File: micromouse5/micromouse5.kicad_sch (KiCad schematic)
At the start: 21 parts, among them J1 Conn_01x06_Pin, J2 Conn_01x06_Pin, J3 JST 2, J4 JST 1, Q1 IR Receiver, U1 HBridge, U2 Voltage Regulator, U3 MOSFET

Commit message: fix naming
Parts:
- R1: footprint micromouse5:BO_CR0805 -> micromouse5:BO_CR0805(51 ohm)
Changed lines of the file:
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@@
 			)
 		)
-		(property "Footprint" "micromouse5:BO_CR0805"
+		(property "Footprint" "micromouse5:BO_CR0805(51 ohm)"
 			(at 237.49 97.79 0)
 			(effects

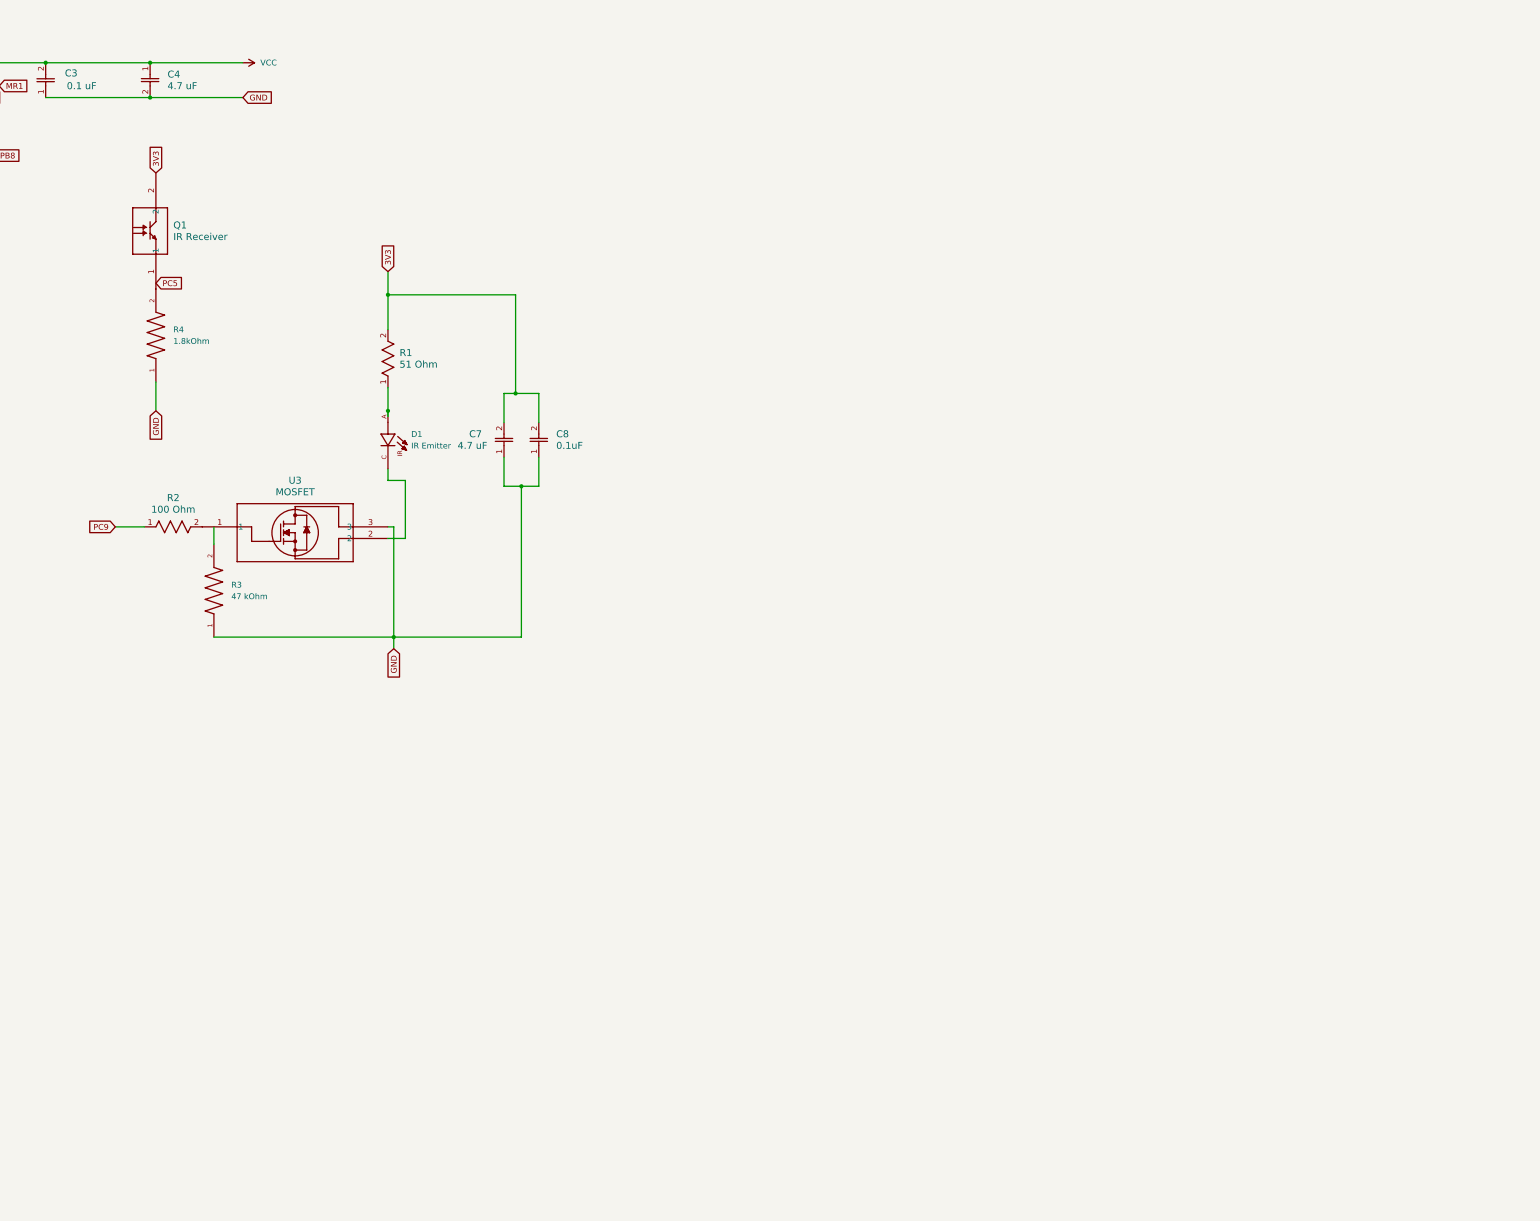
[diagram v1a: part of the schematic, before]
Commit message: Increased size of schematic and created groups/text labels
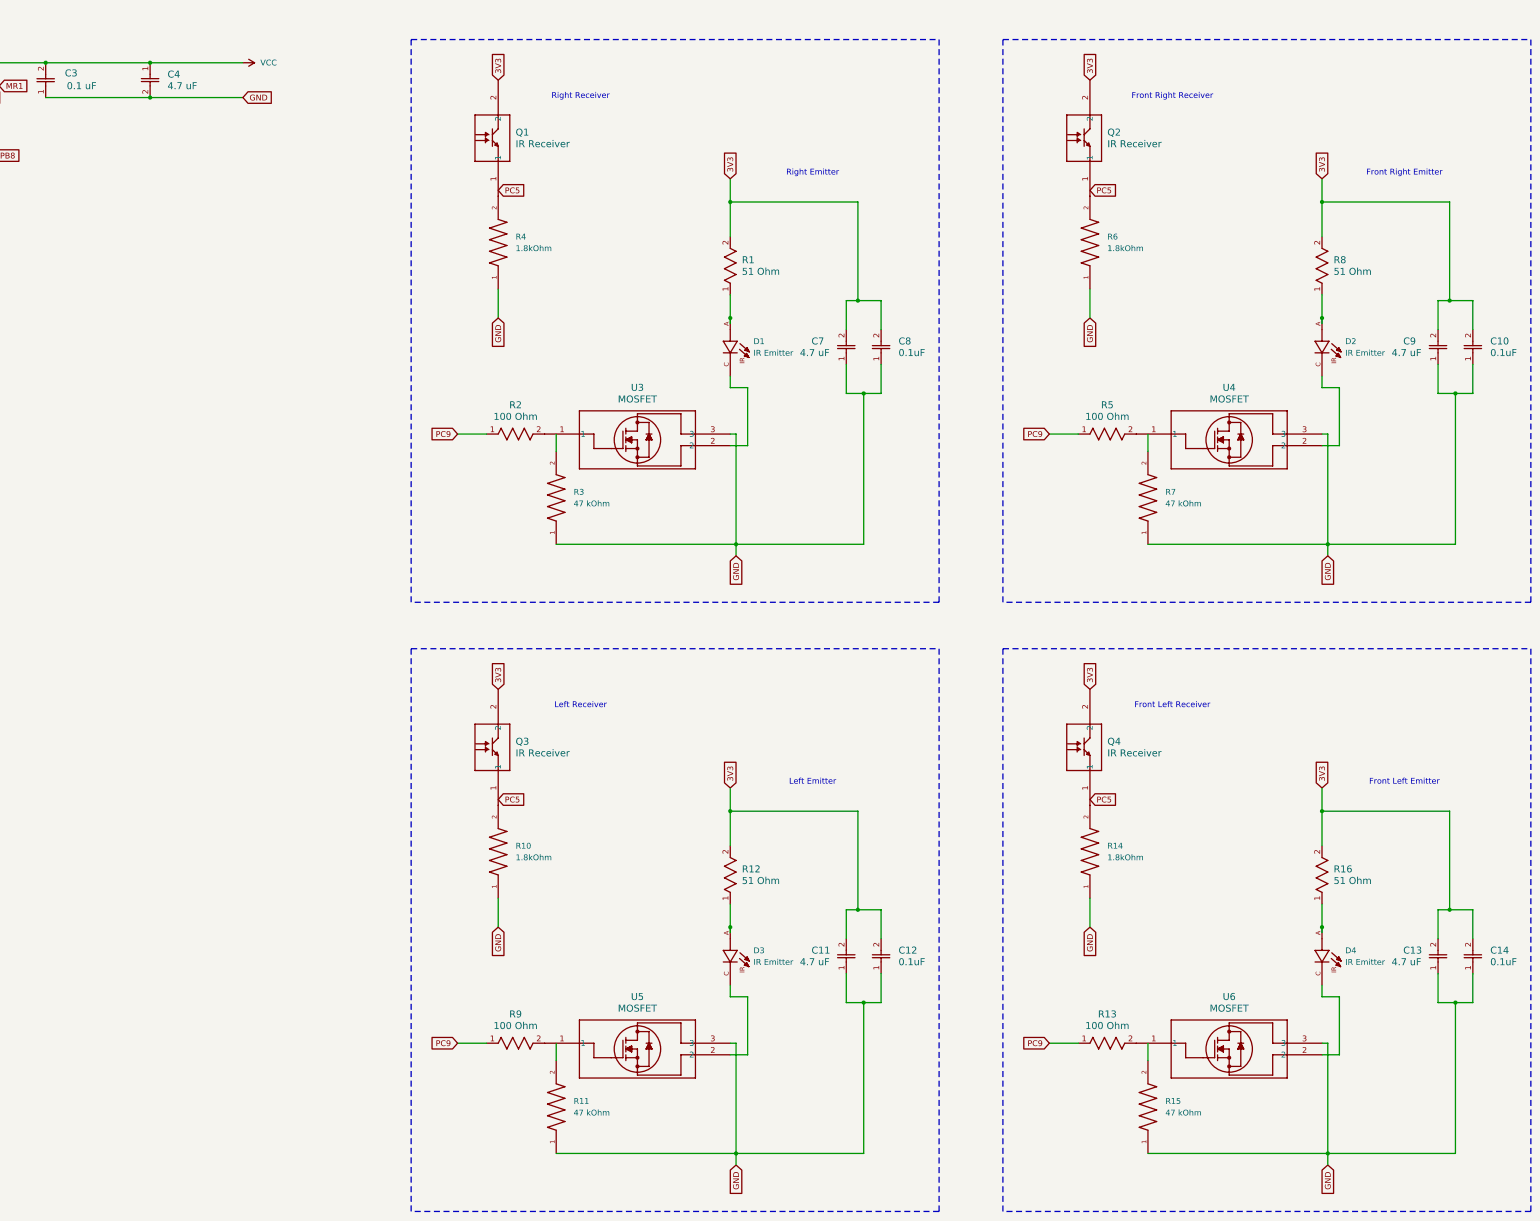
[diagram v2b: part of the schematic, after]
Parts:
- added C10, C12, C14: 0.1uF, micromouse5:G-21_MUR(0.1), symbol Capacitor-0.1uF:GRM21BR71C475KE51L
- added C11, C13, C9: 4.7 uF, micromouse5:CAP_GRM0805_2X1P25_MUR, symbol Capacitor-4.7uF:GCJ21BR72A104KA01L
- added D2, D3, D4: IR Emitter, micromouse5:DIO_SFH_4545 (IR- Emitter), symbol IR-Emitter:SFH_4545
- added Q2, Q3, Q4: IR Receiver, micromouse5:NoneP157X157-2_LTO (IR- Receiver), symbol IR-Receiver:LTR-4206E
- added R10, R14, R6: 1.8kOhm, micromouse5:RESC2012X60N (1.8kΩ), symbol Resistor- 1.8kohm:RK73H2ATTD1801F
- added R11, R15, R7: 47 kOhm, micromouse5:RESC2012X60N (47kΩ), symbol Resistor- 47kohm:RK73H2ARTTD4702F
- added R12, R16, R8: 51 Ohm, micromouse5:BO_CR0805(51 ohm), symbol CRM0805-FX-51R0ELF (51 ohm):CRM0805-FX-51R0ELF
- added R13, R5, R9: 100 Ohm, micromouse5:STA_RNCP0805_STP(100 ohm), symbol RNCP0805FTD100R(100 resistor):RNCP0805FTD100R
- added U4, U5, U6: MOSFET, micromouse5:SOT-23_3L_ONS (mosfet), symbol Mosfet:2N7002LT1G
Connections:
- net 3V3: now also C10.2, C11.2, C12.2, C13.2, C14.2, C9.2, Q2.2, Q3.2, Q4.2, R12.2, R16.2, R8.2
- net GND: now also C10.1, C11.1, C12.1, C13.1, C14.1, C9.1, R10.1, R11.1, R14.1, R15.1, R6.1, R7.1, U4.3, U5.3, U6.3
- net PC9: now also R13.1, R5.1, R9.1
- new net: D4.A, R16.1
- new net: D4.C, U6.2
- new net: Q4.1, R14.2
- new net: D3.A, R12.1
- new net: D3.C, U5.2
- new net: R5.2, U4.1
- new net: D2.C, U4.2
- new net: Q2.1, R6.2
- new net: R13.2, U6.1
- new net: R9.2, U5.1
- new net: D2.A, R8.1
- new net: Q3.1, R10.2
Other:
- note added: "Front Left Emitter"
- note added: "Front Left Receiver"
- note added: "Front Right Emitter"
- note added: "Front Right Receiver"
- note added: "Left Emitter"
- note added: "Left Receiver"
- note added: "Right Emitter"
- note added: "Right Receiver"
- moved on the sheet: C7, C8, D1, Q1, R1, R2, R3, R4, U3

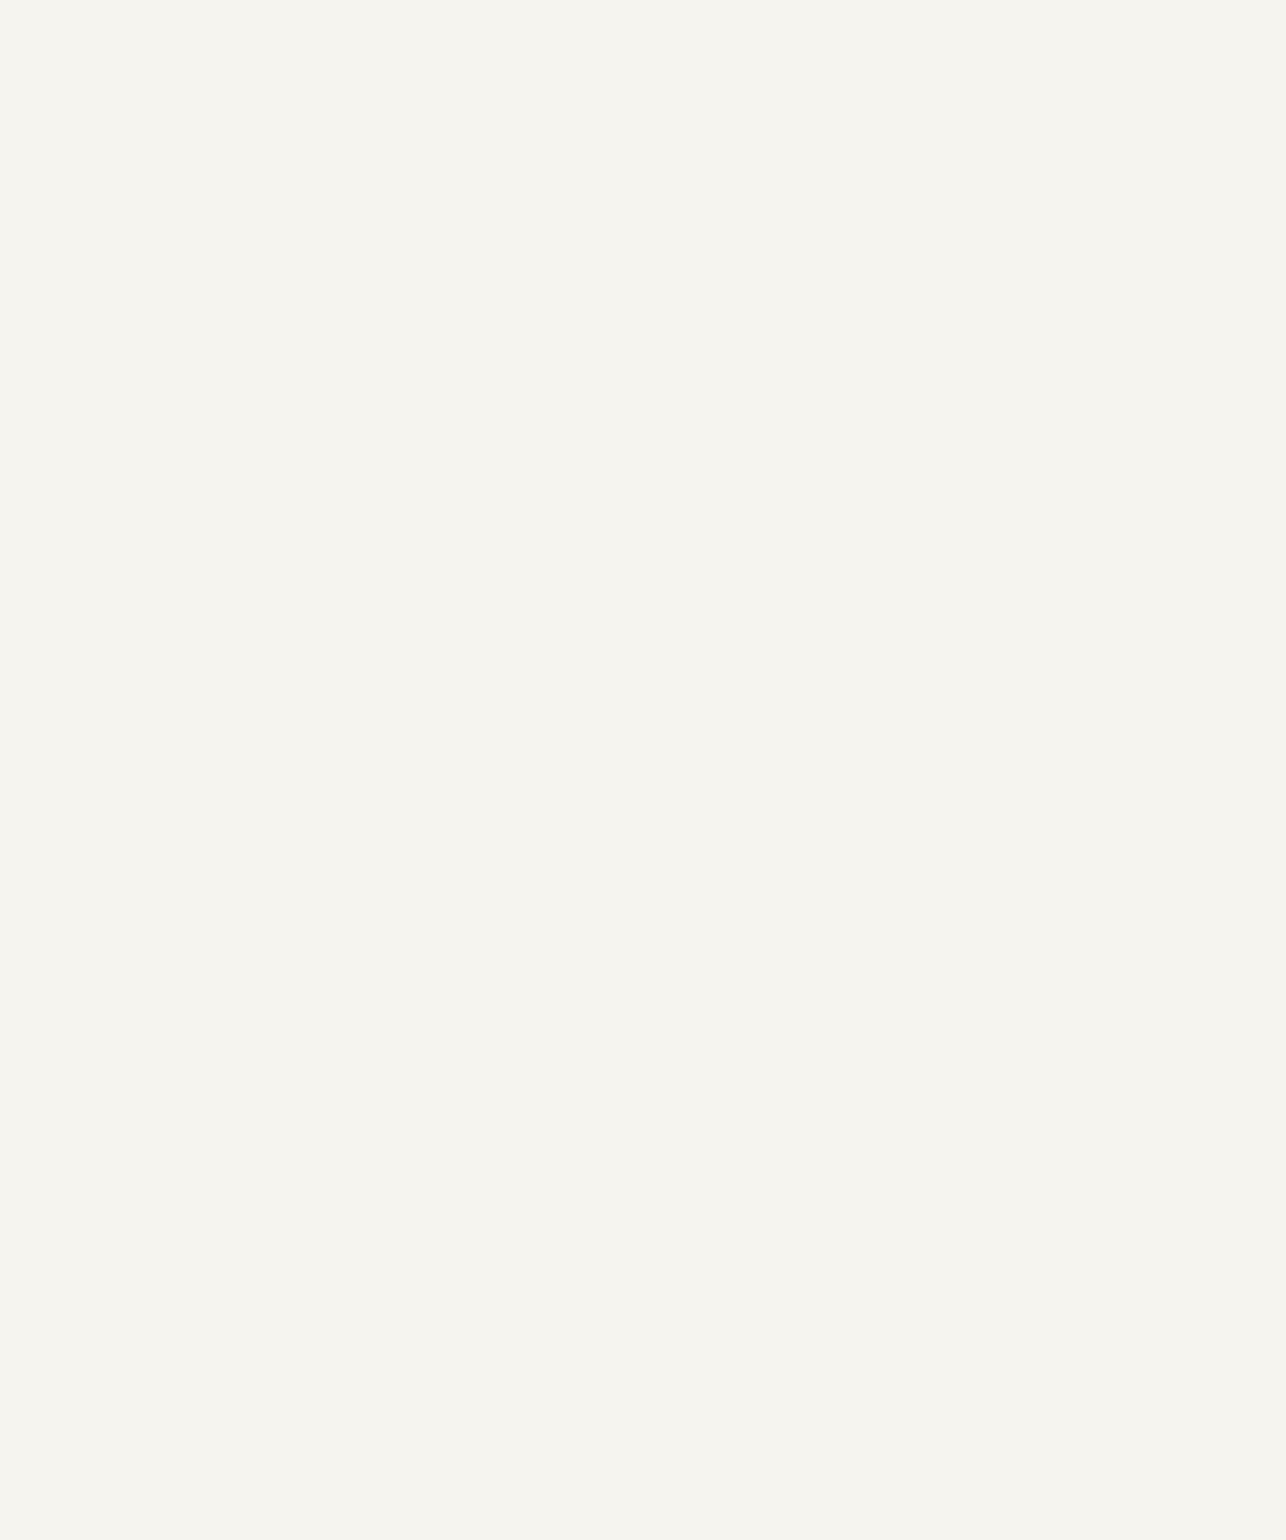
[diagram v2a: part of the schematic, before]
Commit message: Microcontroller addition
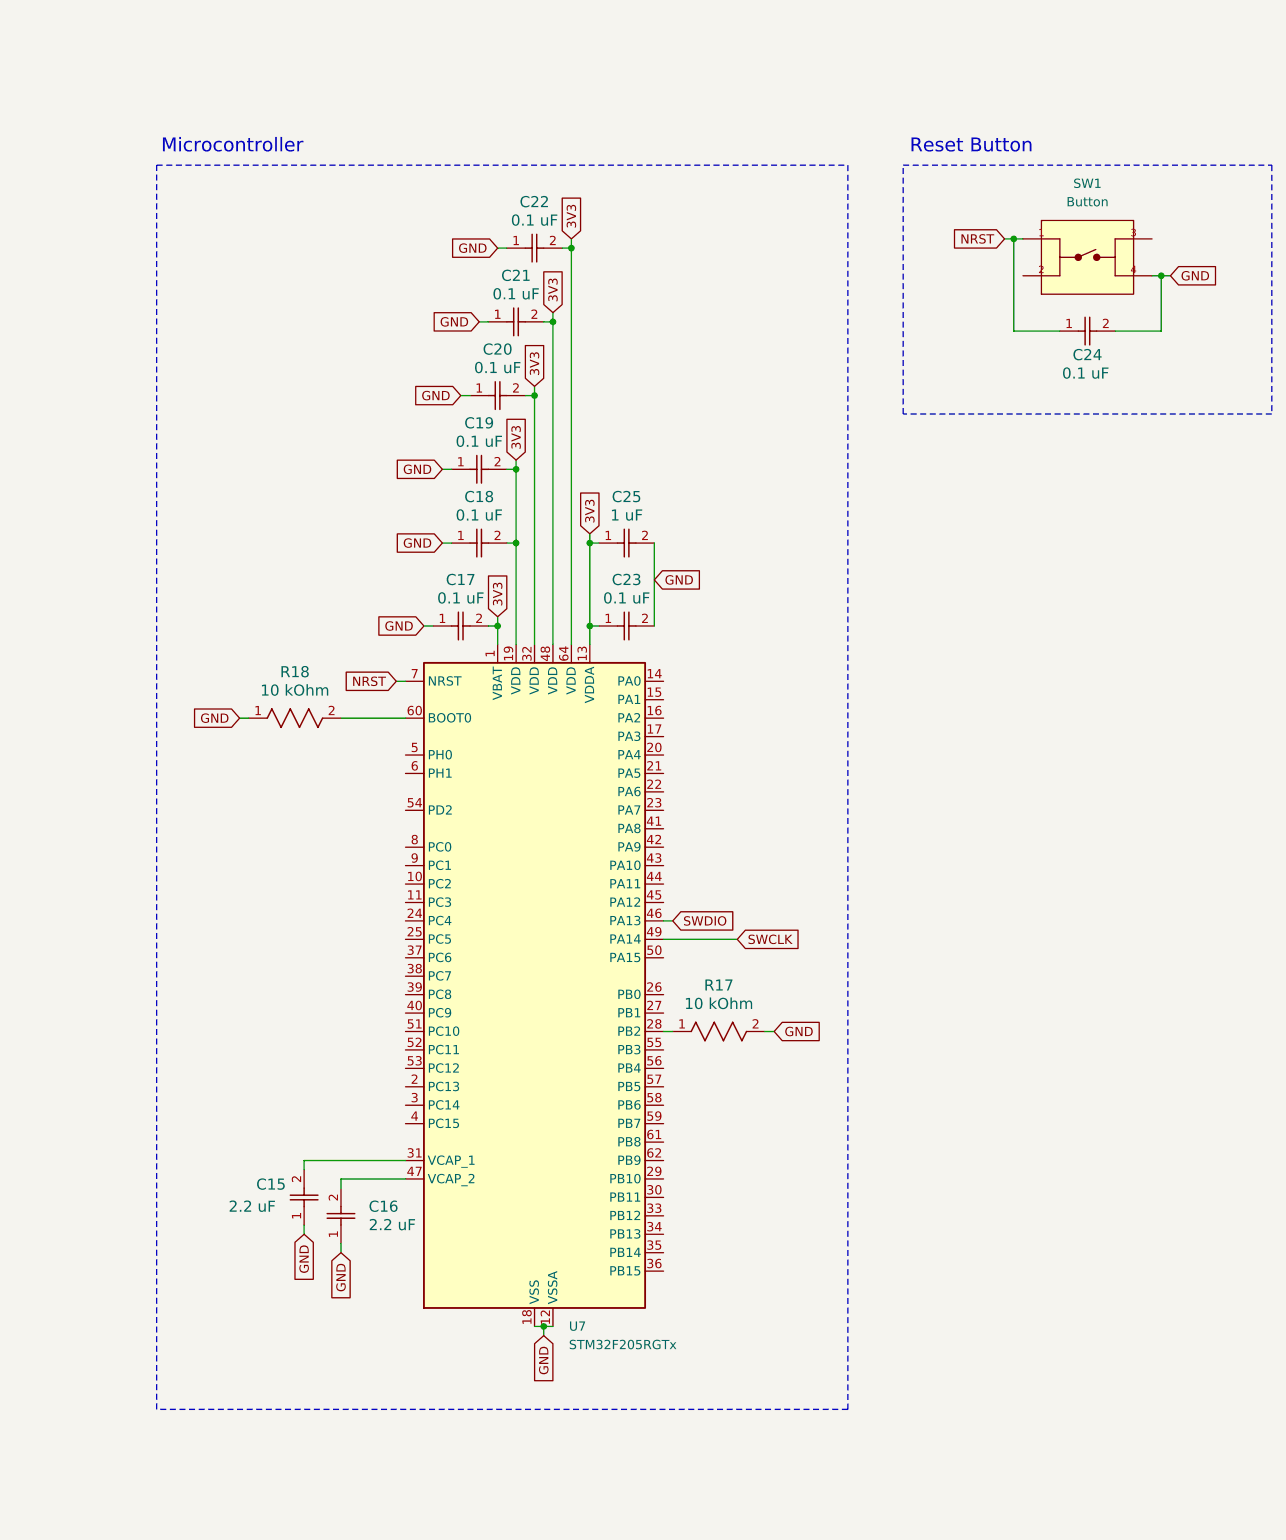
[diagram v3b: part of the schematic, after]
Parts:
- added C15, C16: 2.2 uF, micromouse5:G-21_MUR, symbol GCM21BR71C225KA64L (22):GCM21BR71C225KA64L
- added C17, C18, C19, C20, C21, C22, C23, C24: 0.1 uF, micromouse5:G-21_MUR(0.1), symbol GCJ21BR72A104KA01L(0.1):GCJ21BR72A104KA01L
- added C25: 1 uF, micromouse5:G-21_MUR (1uF), symbol GRM21BR71C105KA01L (1):GRM21BR71C105KA01L
- added R17, R18: 10 kOhm, micromouse5:STA_RNCP0805_STP, symbol RNCP0805FTD10K0 (10k R):RNCP0805FTD10K0
- added SW1: Button, Button_FP_FSM4JSMA:TE_FSM4JSMA, symbol Button_FSM4JSMA:FSM4JSMA
- added U7: STM32F205RGTx, Package_QFP:LQFP-64_10x10mm_P0.5mm, symbol MCU_ST_STM32F2:STM32F205RGTx
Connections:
- net 3V3: now also C17.2, C18.2, C19.2, C20.2, C21.2, C22.2, C23.1, C25.1, U7.1 (VBAT), U7.13 (VDDA), U7.19 (VDD), U7.32 (VDD), U7.48 (VDD), U7.64 (VDD)
- net GND: now also C15.1, C16.1, C17.1, C18.1, C19.1, C20.1, C21.1, C22.1, C23.2, C24.2, C25.2, R17.2, R18.1, SW1.4, U7.12 (VSSA), U7.18 (VSS), U7.63 (VSS)
- new net: C15.2, U7.31 (VCAP_1)
- new net: C16.2, U7.47 (VCAP_2)
- new net: R18.2, U7.60 (BOOT0)
- new net: R17.1, U7.28 (PB2)
- new net NRST: C24.1, SW1.1, U7.7 (NRST)
- new net SWCLK: U7.49 (PA14)
- new net SWDIO: U7.46 (PA13)
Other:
- note added: "Microcontroller"
- note added: "Reset Button"

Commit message: Final cleanup
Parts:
- added J5: Conn_01x04_Pin, symbol Connector:Conn_01x04_Pin
- added SW2: EG1218, SW_1218_EWI, symbol mm_Switch:EG1218
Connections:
- net GND: now also J5.3 (Pin_3)
- net NRST: now also J5.1 (Pin_1)
- net SWCLK: now also J5.4 (Pin_4)
- net SWDIO: now also J5.2 (Pin_2)
- net VCC: now also SW2.1; no longer J3.1
- new net: J3.1, SW2.2
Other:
- moved on the sheet: C15, C16, C17, C18, C19, C20, C21, C22, C23, C24, C25, C5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

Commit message: Updated Labels
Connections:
- net GND: no longer C3.1, C4.2
- net MGND: now also C3.1, C4.2, U1.14 (GND), U1.15 (GND), U1.16 (GND), U1.4 (GND), U1.5 (GND), U1.6 (GND), U1.7 (GND)
- net PC5: now also R13.1
- net Right Emitter: now reaches U7.10 (PC2)
- net Front Right Emitter: now reaches U7.11 (PC3)
- net Right Encoder Ch1: now reaches U7.14 (PA0)
- net Right Encoder Ch2: now reaches U7.15 (PA1)
- net Right Receiver: now reaches U7.17 (PA3)
- net Front Right Receiver: now reaches U7.20 (PA4)
- net Left Receiver: now reaches U7.21 (PA5)
- net Front Left Receiver: now reaches U7.22 (PA6)
- net Left Emitter: now reaches U7.24 (PC4)
- net Front Left Emitter: now reaches U7.25 (PC5)
- net Left Encoder Ch1: now reaches U7.41 (PA8)
- net Left Encoder Ch2: now reaches U7.42 (PA9)
- net Motor: now reaches U7.58 (PB6)
- net Motor: now also U7.59 (PB7), U7.61 (PB8), U7.62 (PB9)
- removed net PC9: R13.1, R2.1, R5.1, R9.1
- new net PC2: R2.1
- new net PC3: R5.1
- new net PC4: R9.1
- no-connect marks 0 -> 32

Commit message: Added light
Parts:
- added D5: LED, symbol Device:LED
- added R19: 47k Ohm, RK73H2ARTTD4702F:RESC2012X60N, symbol Resistor- 47kohm:RK73H2ARTTD4702F
- added R20: 100 Ohm, micromouse5:STA_RNCP0805_STP(100 ohm), symbol RNCP0805FTD100R(100 resistor):RNCP0805FTD100R
- added R21: 300 Ohm, RK73H2ATTD3000F:RESC2012X60N, symbol Resistor- 300ohm:RK73H2ATTD3000F
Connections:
- net 3V3: now also R19.1
- net GND: now also R20.2, R21.2; no longer C24.2
- net Power Status LED: now reaches U7.52 (PC11)
- net at SW1.2: now also R19.2
- new net: D5.1 (K), R21.1
- new net: C24.2, R20.1
- new net PC11: D5.2 (A)
- no-connect marks 32 -> 31
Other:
- note added: "Power Status LED"
- moved on the sheet: C24, J5, SW1
